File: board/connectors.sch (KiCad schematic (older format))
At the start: 4 parts

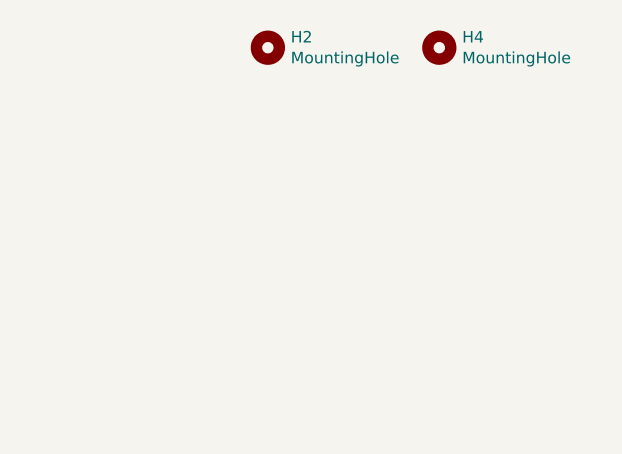
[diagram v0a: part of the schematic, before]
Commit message: Rework on power supply and added pressure sensor
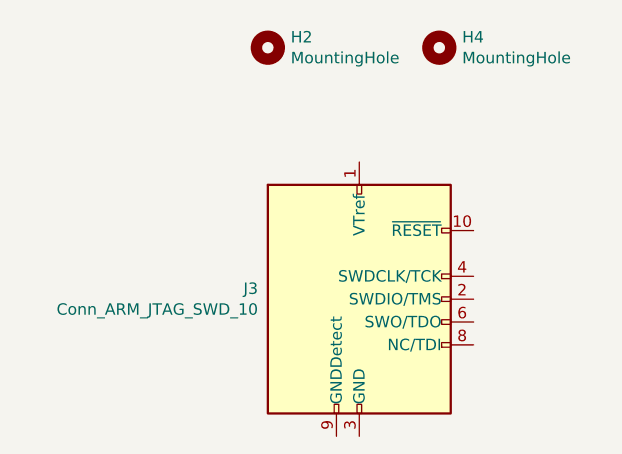
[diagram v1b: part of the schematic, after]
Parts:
- added J3: Conn_ARM_JTAG_SWD_10, symbol Connector:Conn_ARM_JTAG_SWD_10
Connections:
- new net: J3.3 (GND), J3.5 (GND)
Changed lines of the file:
@@
+	1    0    0    -1
+$EndComp
+$Comp
+L Connector:Conn_ARM_JTAG_SWD_10 J3
+U 1 1 60A4A004
+P 5200 3250
+F 0 "J3" H 4757 3296 50  0000 R CNN
+F 1 "Conn_ARM_JTAG_SWD_10" H 4757 3205 50  0000 R CNN
+F 2 "" H 5200 3250 50  0001 C CNN
+F 3 "http://infocenter.arm.com/help/topic/com.arm.doc.ddi0314h/DDI0314H_coresight_components_trm.pdf" V 4850 2000 50  0001 C CNN
+	1    5200 3250
 	1    0    0    -1
 $EndComp

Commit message: Update
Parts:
- added J2: USB_B_Micro, Connector_USB:USB_Micro-B_Amphenol_10103594-0001LF_Horizontal, symbol board-rescue:USB_B_Micro-Connector
- added U6: USBLC6-2SC6, Package_TO_SOT_SMD:SOT-23-6, symbol Power_Protection:USBLC6-2SC6
- J3: footprint (none) -> Connector_PinHeader_1.27mm:PinHeader_2x05_P1.27mm_Vertical_SMD
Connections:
- new net GND: J2.5 (GND), U6.2 (GND)
- new net USB_CONN_D+: J2.3 (D+), U6.3 (I/O2)
- new net USB_CONN_D-: J2.2 (D-), U6.1 (I/O1)
- new net USB_D+: U6.4 (I/O2)
- new net USB_D-: U6.6 (I/O1)
- new net VBUS: J2.1 (VBUS), U6.5 (VBUS)
- no-connect marks 0 -> 2
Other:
- note added: "USB"
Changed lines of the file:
@@
 F 0 "J3" H 4757 3296 50  0000 R CNN
 F 1 "Conn_ARM_JTAG_SWD_10" H 4757 3205 50  0000 R CNN
-F 2 "" H 5200 3250 50  0001 C CNN
+F 2 "Connector_PinHeader_1.27mm:PinHeader_2x05_P1.27mm_Vertical_SMD" H 5200 3250 50  0001 C CNN
 F 3 "http://infocenter.arm.com/help/topic/com.arm.doc.ddi0314h/DDI0314H_coresight_components_trm.pdf" V 4850 2000 50  0001 C CNN
 	1    5200 3250
 	1    0    0    -1
 $EndComp
+$Comp
+L board-rescue:USB_B_Micro-Connector J2
+U 1 1 60B231B3
+P 3800 5400
+F 0 "J2" H 3857 5867 50  0000 C CNN
+F 1 "USB_B_Micro" H 3857 5776 50  0000 C CNN
+F 2 "Connector_USB:USB_Micro-B_Amphenol_10103594-0001LF_Horizontal" H 3950 5350 50  0001 C CNN
+F 3 "~" H 3950 5350 50  0001 C CNN
+	1    3800 5400
+	1    0    0    -1
+$EndComp
+$Comp
+L power:GND #PWR041
+U 1 1 60B231B9
+P 3800 5800
+F 0 "#PWR041" H 3800 5550 50  0001 C CNN
+F 1 "GND" H 3805 5627 50  0000 C CNN
+F 2 "" H 3800 5800 50  0001 C CNN
+F 3 "" H 3800 5800 50  0001 C CNN
+	1    3800 5800
+	1    0    0    -1
+$EndComp
+NoConn ~ 3700 5800
+$Comp
+L power:VBUS #PWR042
+U 1 1 60B231C0
+P 4200 5050
+F 0 "#PWR042" H 4200 4900 50  0001 C CNN
+F 1 "VBUS" H 4215 5223 50  0000 C CNN
+F 2 "" H 4200 5050 50  0001 C CNN
+F 3 "" H 4200 5050 50  0001 C CNN
+	1    4200 5050
+	1    0    0    -1
+$EndComp
+Wire Wire Line
+	4200 5050 4200 5200
+Wire Wire Line
+	4200 5200 4100 5200
+Text GLabel 4100 5400 2    50   Input ~ 0
+USB_CONN_D+
+Text GLabel 4100 5500 2    50   Input ~ 0
+USB_CONN_D-
+NoConn ~ 4100 5600
+$Comp
+L Power_Protection:USBLC6-2SC6 U6
+U 1 1 60B231CB
+P 2200 5400
+F 0 "U6" H 2450 5800 50  0000 C CNN
+F 1 "USBLC6-2SC6" H 2550 5050 50  0000 C CNN
+F 2 "Package_TO_SOT_SMD:SOT-23-6" H 2200 4900 50  0001 C CNN
+F 3 "https://www.st.com/resource/en/datasheet/usblc6-2.pdf" H 2400 5750 50  0001 C CNN
+	1    2200 5400
+	1    0    0    -1
+$EndComp
+$Comp
+L power:VBUS #PWR039
+U 1 1 60B231D1
+P 2200 5000
+F 0 "#PWR039" H 2200 4850 50  0001 C CNN
+F 1 "VBUS" H 2200 5150 50  0000 C CNN
+F 2 "" H 2200 5000 50  0001 C CNN
+F 3 "" H 2200 5000 50  0001 C CNN
+	1    2200 5000
+	1    0    0    -1
+$EndComp
+Text GLabel 2600 5300 2    50   Input ~ 0
+USB_D+
+Text GLabel 1800 5300 0    50   Input ~ 0
+USB_D-
+Text GLabel 2600 5500 2    50   Input ~ 0
+USB_CONN_D+
+Text GLabel 1800 5500 0    50   Input ~ 0
+USB_CONN_D-
+$Comp
+L power:GND #PWR040
+U 1 1 60B231DB
+P 2200 5800
+F 0 "#PWR040" H 2200 5550 50  0001 C CNN
+F 1 "GND" H 2205 5627 50  0000 C CNN
+F 2 "" H 2200 5800 50  0001 C CNN
+F 3 "" H 2200 5800 50  0001 C CNN
+	1    2200 5800
+	1    0    0    -1
+$EndComp
+Wire Notes Line
+	4750 6050 1100 6050
+Wire Notes Line
+	1100 6050 1100 4550
+Wire Notes Line
+	1100 4550 4750 4550
+Wire Notes Line
+	4750 4550 4750 6050
+Text Notes 4500 4650 0    50   ~ 0
+USB
 $EndSCHEMATC

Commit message: Generic update
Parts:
- added C27: C_Small, Capacitor_SMD:C_0402_1005Metric, symbol Device:C_Small
- added J4, J5, J?: Conn_01x02_Male, Connector_PinHeader_2.54mm:PinHeader_1x02_P2.54mm_Vertical_SMD_Pin1Right, symbol Connector:Conn_01x02_Male
- added R16, R17, R18, R19, R20: 100, Resistor_SMD:R_0603_1608Metric, symbol Device:R_Small_US
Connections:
- net labels added: +3.3V, SWD_!RESET, SWD_TCK, SWD_TDI, SWD_TDO, SWD_TMS
- wire segments 2 -> 19
- no-connect marks 2 -> 3
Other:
- note added: "12V power in"
- note added: "5V PWR OUT\nGND"
- note added: "Decoupling filter for reset pin ??????\n"
- note added: "Mounting holes\n"
- note added: "SWD\n"
- note added: "USART\n"
- moved on the sheet: H1, H2, H3, H4, J3

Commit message: Updated schematic
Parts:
- removed J4, J5, J?: Conn_01x02_Male, Connector_PinHeader_2.54mm:PinHeader_1x02_P2.54mm_Vertical_SMD_Pin1Right, symbol Connector:Conn_01x02_Male
- removed R17: 100, Resistor_SMD:R_0603_1608Metric, symbol Device:R_Small_US
- added J4: Conn_01x04_Male, symbol Connector:Conn_01x04_Male
- added J5: Screw_Terminal_01x02, symbol Connector:Screw_Terminal_01x02
- C30: renamed from C27; value C_Small -> 100n
- R20: renamed from R19; value 100 -> 10k
- renumbered J3 to J2, J2 to J3, R16 to R18, R18 to R19, R20 to R21
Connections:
- net labels added: +5V, 12V_IN, SWDCLK, SWDIO, SWO, USART3_RX, USART3_TX
- net labels removed: SWD_TCK, SWD_TDI, SWD_TDO, SWD_TMS
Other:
- note added: "Connectors"
- note added: "External Connectors\n"
- note added: "Serial Wire Debug\n"
- note removed: "12V power in"
- note removed: "5V PWR OUT\nGND"
- note removed: "SWD\n"
- note removed: "USART\n"
- moved on the sheet: C30, H1, H2, H3, H4, J2, J3, R18, R19, R20, R21, U6

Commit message: Updated schematic
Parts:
- removed R20: 10k, Resistor_SMD:R_0603_1608Metric, symbol Device:R_Small_US
- added R? (x3): 22, Resistor_SMD:R_0603_1608Metric, symbol Device:R_Small_US
- R18, R19, R21: value 100 -> 22
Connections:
- net USART3_RX: now also R?.1; no longer J4.3 (Pin_3)
- net USART3_TX: now also R?.1; no longer J4.2 (Pin_2)
- net 12V_IN renamed +12V
- net SWD_!RESET: no longer names the net of J2.10 (~RESET~)
- net SWD_!RESET: now also R?.1; no longer C30.1
- new net: J4.2 (Pin_2), R?.2
- new net: J4.3 (Pin_3), R?.2
- new net NRST: C30.1, R?.2
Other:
- note removed: "Decoupling filter for reset pin ??????\n"
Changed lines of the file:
@@
 P 4350 4550
 F 0 "R21" V 4300 4450 50  0000 C CNN
-F 1 "100" V 4300 4650 50  0000 C CNN
+F 1 "22" V 4300 4650 50  0000 C CNN
 F 2 "Resistor_SMD:R_0603_1608Metric" H 4350 4550 50  0001 C CNN
 F 3 "~" H 4350 4550 50  0001 C CNN
@@
 P 3900 4450
 F 0 "R18" V 3800 4350 50  0000 C CNN
-F 1 "100" V 3800 4500 50  0000 C CNN
+F 1 "22" V 3800 4500 50  0000 C CNN
 F 2 "Resistor_SMD:R_0603_1608Metric" H 3900 4450 50  0001 C CNN
 F 3 "~" H 3900 4450 50  0001 C CNN
@@
 U 1 1 60B2FE42
 P 4000 4650
-F 0 "R19" V 3950 4550 50  0000 C CNN
-F 1 "100" V 3950 4750 50  0000 C CNN
+F 0 "R19" V 4100 4550 50  0000 C CNN
+F 1 "22" V 4100 4750 50  0000 C CNN
 F 2 "Resistor_SMD:R_0603_1608Metric" H 4000 4650 50  0001 C CNN
 F 3 "~" H 4000 4650 50  0001 C CNN
@@
 	0    1    1    0
 $EndComp
-Text Notes 2650 3350 0    50   ~ 0
-Decoupling filter for reset pin ??????\n
 Wire Wire Line
 	3800 4450 3700 4450
@@
 	3200 5200 3200 5150
 Text GLabel 4600 3900 2    50   Input ~ 0
-SWD_!RESET
+NRST
 $Comp
 L Device:C_Small C30
@@
 $EndComp
 Wire Wire Line
-	3700 4250 3850 4250
-Wire Wire Line
-	3850 4250 3850 3900
-Wire Wire Line
 	3850 3900 4350 3900
 Wire Wire Line
@@
 Wire Wire Line
 	4350 3900 4600 3900
-$Comp
-L Device:R_Small_US R20
-U 1 1 60B3DCEE
-P 4350 3700
-F 0 "R20" V 4250 3600 50  0000 C CNN
-F 1 "10k" V 4250 3750 50  0000 C CNN
-F 2 "Resistor_SMD:R_0603_1608Metric" H 4350 3700 50  0001 C CNN
-F 3 "~" H 4350 3700 50  0001 C CNN
-	1    4350 3700
-	-1   0    0    1
-$EndComp
-Wire Wire Line
-	4350 3800 4350 3900
-$Comp
-L power:+3.3V #PWR050
-U 1 1 60B3ECAF
-P 4350 3550
-F 0 "#PWR050" H 4350 3400 50  0001 C CNN
-F 1 "+3.3V" H 4365 3723 50  0000 C CNN
-F 2 "" H 4350 3550 50  0001 C CNN
-F 3 "" H 4350 3550 50  0001 C CNN
-	1    4350 3550
-	1    0    0    -1
-$EndComp
-Wire Wire Line
-	4350 3550 4350 3600
 $Comp
 L power:+3.3V #PWR047
@@
 Text Notes 4500 3250 0    50   ~ 0
 Serial Wire Debug\n
-Text GLabel 6150 2000 2    50   Input ~ 0
+Text GLabel 6400 2000 2    50   Input ~ 0
 USART3_TX
-Text GLabel 6150 2100 2    50   Input ~ 0
+Text GLabel 6400 2100 2    50   Input ~ 0
 USART3_RX
 $Comp
@@
 	1    0    0    -1
 $EndComp
-Text GLabel 5950 2550 0    50   Input ~ 0
-12V_IN
 $Comp
 L Connector:Screw_Terminal_01x02 J5
@@
 U 1 1 60CCE439
 P 5950 2000
-F 0 "J4" H 6500 2250 50  0000 C CNN
-F 1 "Conn_01x04_Male" H 6550 2150 50  0000 C CNN
+F 0 "J4" H 6450 2300 50  0000 C CNN
+F 1 "Conn_01x04_Male" H 6600 2250 50  0000 C CNN
 F 2 "" H 5950 2000 50  0001 C CNN
 F 3 "~" H 5950 2000 50  0001 C CNN
@@
 Text Notes 7150 6950 0    217  ~ 43
 Connectors
+$Comp
+L Device:R_Small_US R?
+U 1 1 60B65AA2
+P 3850 4100
+F 0 "R?" V 3750 4000 50  0000 C CNN
+F 1 "22" V 3750 4150 50  0000 C CNN
+F 2 "Resistor_SMD:R_0603_1608Metric" H 3850 4100 50  0001 C CNN
+F 3 "~" H 3850 4100 50  0001 C CNN
+	1    3850 4100
+	-1   0    0    1
+$EndComp
+Wire Wire Line
+	3700 4250 3850 4250
+Wire Wire Line
+	3850 4250 3850 4200
+Wire Wire Line
+	3850 3900 3850 4000
+$Comp
+L Device:R_Small_US R?
+U 1 1 60B676F2
+P 6300 2000
+F 0 "R?" V 6200 1950 50  0000 C CNN
+F 1 "22" V 6200 2100 50  0000 C CNN
+F 2 "Resistor_SMD:R_0603_1608Metric" H 6300 2000 50  0001 C CNN
+F 3 "~" H 6300 2000 50  0001 C CNN
+	1    6300 2000
+	0    1    1    0
+$EndComp
+Wire Wire Line
+	6200 2000 6150 2000
+$Comp
+L Device:R_Small_US R?
+U 1 1 60B68FD5
+P 6300 2100
+F 0 "R?" V 6400 2050 50  0000 C CNN
+F 1 "22" V 6400 2200 50  0000 C CNN
+F 2 "Resistor_SMD:R_0603_1608Metric" H 6300 2100 50  0001 C CNN
+F 3 "~" H 6300 2100 50  0001 C CNN
+	1    6300 2100
+	0    1    1    0
+$EndComp
+Wire Wire Line
+	6200 2100 6150 2100
+$Comp
+L power:+12V #PWR?
+U 1 1 60B819F2
+P 5800 2450
+F 0 "#PWR?" H 5800 2300 50  0001 C CNN
+F 1 "+12V" H 5815 2623 50  0000 C CNN
+F 2 "" H 5800 2450 50  0001 C CNN
+F 3 "" H 5800 2450 50  0001 C CNN
+	1    5800 2450
+	1    0    0    -1
+$EndComp
+Wire Wire Line
+	5800 2450 5800 2550
+Wire Wire Line
+	5800 2550 5950 2550
 $EndSCHEMATC

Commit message: Updated footprints
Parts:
- J4: footprint (none) -> Connector_PinHeader_2.54mm:PinHeader_1x04_P2.54mm_Vertical
- J5: footprint (none) -> TerminalBlock_Phoenix:TerminalBlock_Phoenix_PT-1,5-2-5.0-H_1x02_P5.00mm_Horizontal
- gave numbers to parts that had none: 3
- renumbered C30 to C33, R18 to R19, R19 to R20
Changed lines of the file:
@@
 $EndComp
 $Comp
-L power:GND #PWR049
+L power:GND #PWR059
 U 1 1 60B231B9
 P 4000 2700
-F 0 "#PWR049" H 4000 2450 50  0001 C CNN
+F 0 "#PWR059" H 4000 2450 50  0001 C CNN
 F 1 "GND" H 4005 2527 50  0000 C CNN
 F 2 "" H 4000 2700 50  0001 C CNN
@@
 NoConn ~ 3900 2700
 $Comp
-L power:VBUS #PWR052
+L power:VBUS #PWR061
 U 1 1 60B231C0
 P 4400 1950
-F 0 "#PWR052" H 4400 1800 50  0001 C CNN
+F 0 "#PWR061" H 4400 1800 50  0001 C CNN
 F 1 "VBUS" H 4415 2123 50  0000 C CNN
 F 2 "" H 4400 1950 50  0001 C CNN
@@
 $EndComp
 $Comp
-L power:VBUS #PWR045
+L power:VBUS #PWR055
 U 1 1 60B231D1
 P 2650 1950
-F 0 "#PWR045" H 2650 1800 50  0001 C CNN
+F 0 "#PWR055" H 2650 1800 50  0001 C CNN
 F 1 "VBUS" H 2650 2100 50  0000 C CNN
 F 2 "" H 2650 1950 50  0001 C CNN
@@
 USB_CONN_D-
 $Comp
-L power:GND #PWR046
+L power:GND #PWR056
 U 1 1 60B231DB
 P 2650 2750
-F 0 "#PWR046" H 2650 2500 50  0001 C CNN
+F 0 "#PWR056" H 2650 2500 50  0001 C CNN
 F 1 "GND" H 2655 2577 50  0000 C CNN
 F 2 "" H 2650 2750 50  0001 C CNN
@@
 $EndComp
 $Comp
-L Device:R_Small_US R18
+L Device:R_Small_US R19
 U 1 1 60B2FA94
 P 3900 4450
-F 0 "R18" V 3800 4350 50  0000 C CNN
+F 0 "R19" V 3800 4350 50  0000 C CNN
 F 1 "22" V 3800 4500 50  0000 C CNN
 F 2 "Resistor_SMD:R_0603_1608Metric" H 3900 4450 50  0001 C CNN
@@
 $EndComp
 $Comp
-L Device:R_Small_US R19
+L Device:R_Small_US R20
 U 1 1 60B2FE42
 P 4000 4650
-F 0 "R19" V 4100 4550 50  0000 C CNN
+F 0 "R20" V 4100 4550 50  0000 C CNN
 F 1 "22" V 4100 4750 50  0000 C CNN
 F 2 "Resistor_SMD:R_0603_1608Metric" H 4000 4650 50  0001 C CNN
@@
 	4250 4550 3700 4550
 $Comp
-L power:GND #PWR048
+L power:GND #PWR058
 U 1 1 60B3B301
 P 3200 5200
-F 0 "#PWR048" H 3200 4950 50  0001 C CNN
+F 0 "#PWR058" H 3200 4950 50  0001 C CNN
 F 1 "GND" H 3205 5027 50  0000 C CNN
 F 2 "" H 3200 5200 50  0001 C CNN
@@
 NRST
 $Comp
-L Device:C_Small C30
+L Device:C_Small C33
 U 1 1 60B3C3D4
 P 4350 4050
-F 0 "C30" H 4442 4096 50  0000 L CNN
+F 0 "C33" H 4442 4096 50  0000 L CNN
 F 1 "100n" H 4442 4005 50  0000 L CNN
 F 2 "Capacitor_SMD:C_0402_1005Metric" H 4350 4050 50  0001 C CNN
@@
 $EndComp
 $Comp
-L power:GND #PWR051
+L power:GND #PWR060
 U 1 1 60B3CC4D
 P 4350 4150
-F 0 "#PWR051" H 4350 3900 50  0001 C CNN
+F 0 "#PWR060" H 4350 3900 50  0001 C CNN
 F 1 "GND" H 4355 3977 50  0000 C CNN
 F 2 "" H 4350 4150 50  0001 C CNN
@@
 	4350 3900 4600 3900
 $Comp
-L power:+3.3V #PWR047
+L power:+3.3V #PWR057
 U 1 1 60B3F606
 P 3200 3850
-F 0 "#PWR047" H 3200 3700 50  0001 C CNN
+F 0 "#PWR057" H 3200 3700 50  0001 C CNN
 F 1 "+3.3V" H 3215 4023 50  0000 C CNN
 F 2 "" H 3200 3850 50  0001 C CNN
@@
 USART3_RX
 $Comp
-L power:GND #PWR053
+L power:GND #PWR063
 U 1 1 60BAA5F2
 P 5950 2650
-F 0 "#PWR053" H 5950 2400 50  0001 C CNN
+F 0 "#PWR063" H 5950 2400 50  0001 C CNN
 F 1 "GND" H 5950 2500 50  0000 C CNN
 F 2 "" H 5950 2650 50  0001 C CNN
@@
 F 0 "J5" H 6250 2550 50  0000 L CNN
 F 1 "Screw_Terminal_01x02" H 6250 2450 50  0000 L CNN
-F 2 "" H 6150 2550 50  0001 C CNN
+F 2 "TerminalBlock_Phoenix:TerminalBlock_Phoenix_PT-1,5-2-5.0-H_1x02_P5.00mm_Horizontal" H 6150 2550 50  0001 C CNN
 F 3 "~" H 6150 2550 50  0001 C CNN
 	1    6150 2550
@@
 F 0 "J4" H 6450 2300 50  0000 C CNN
 F 1 "Conn_01x04_Male" H 6600 2250 50  0000 C CNN
-F 2 "" H 5950 2000 50  0001 C CNN
+F 2 "Connector_PinHeader_2.54mm:PinHeader_1x04_P2.54mm_Vertical" H 5950 2000 50  0001 C CNN
 F 3 "~" H 5950 2000 50  0001 C CNN
 	1    5950 2000
@@
 $EndComp
 $Comp
-L power:GND #PWR055
+L power:GND #PWR065
 U 1 1 60CCF70F
 P 6150 2200
-F 0 "#PWR055" H 6150 1950 50  0001 C CNN
+F 0 "#PWR065" H 6150 1950 50  0001 C CNN
 F 1 "GND" H 6150 2050 50  0000 C CNN
 F 2 "" H 6150 2200 50  0001 C CNN
@@
 $EndComp
 $Comp
-L power:+5V #PWR054
+L power:+5V #PWR064
 U 1 1 60CCFD5D
 P 6150 1850
-F 0 "#PWR054" H 6150 1700 50  0001 C CNN
+F 0 "#PWR064" H 6150 1700 50  0001 C CNN
 F 1 "+5V" H 6165 2023 50  0000 C CNN
 F 2 "" H 6150 1850 50  0001 C CNN
@@
 Connectors
 $Comp
-L Device:R_Small_US R?
+L Device:R_Small_US R18
 U 1 1 60B65AA2
 P 3850 4100
-F 0 "R?" V 3750 4000 50  0000 C CNN
+F 0 "R18" V 3750 4000 50  0000 C CNN
 F 1 "22" V 3750 4150 50  0000 C CNN
 F 2 "Resistor_SMD:R_0603_1608Metric" H 3850 4100 50  0001 C CNN
@@
 	3850 3900 3850 4000
 $Comp
-L Device:R_Small_US R?
+L Device:R_Small_US R22
 U 1 1 60B676F2
 P 6300 2000
-F 0 "R?" V 6200 1950 50  0000 C CNN
+F 0 "R22" V 6200 1950 50  0000 C CNN
 F 1 "22" V 6200 2100 50  0000 C CNN
 F 2 "Resistor_SMD:R_0603_1608Metric" H 6300 2000 50  0001 C CNN
@@
 	6200 2000 6150 2000
 $Comp
-L Device:R_Small_US R?
+L Device:R_Small_US R23
 U 1 1 60B68FD5
 P 6300 2100
-F 0 "R?" V 6400 2050 50  0000 C CNN
+F 0 "R23" V 6400 2050 50  0000 C CNN
 F 1 "22" V 6400 2200 50  0000 C CNN
 F 2 "Resistor_SMD:R_0603_1608Metric" H 6300 2100 50  0001 C CNN
@@
 	6200 2100 6150 2100
 $Comp
-L power:+12V #PWR?
+L power:+12V #PWR062
 U 1 1 60B819F2
 P 5800 2450
-F 0 "#PWR?" H 5800 2300 50  0001 C CNN
+F 0 "#PWR062" H 5800 2300 50  0001 C CNN
 F 1 "+12V" H 5815 2623 50  0000 C CNN
 F 2 "" H 5800 2450 50  0001 C CNN

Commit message: Update
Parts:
- J3: footprint Connector_USB:USB_Micro-B_Amphenol_10103594-0001LF_Horizontal -> Connector_USB:USB_Micro-B_Molex_47346-0001
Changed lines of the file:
@@
 F 0 "J3" H 4057 2767 50  0000 C CNN
 F 1 "USB_B_Micro" H 4057 2676 50  0000 C CNN
-F 2 "Connector_USB:USB_Micro-B_Amphenol_10103594-0001LF_Horizontal" H 4150 2250 50  0001 C CNN
+F 2 "Connector_USB:USB_Micro-B_Molex_47346-0001" H 4150 2250 50  0001 C CNN
 F 3 "~" H 4150 2250 50  0001 C CNN
 	1    4000 2300

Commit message: ok
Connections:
- net USART3_RX: now also R22.1; no longer R23.1
- net USART3_TX: now also R23.1; no longer R22.1
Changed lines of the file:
@@
 Text Notes 4500 3250 0    50   ~ 0
 Serial Wire Debug\n
+Text GLabel 6400 2100 2    50   Input ~ 0
+USART3_TX
 Text GLabel 6400 2000 2    50   Input ~ 0
-USART3_TX
-Text GLabel 6400 2100 2    50   Input ~ 0
 USART3_RX
 $Comp
